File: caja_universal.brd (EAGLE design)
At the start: 136.8 x 101.5 mm, 45 parts, among them IC1 NE5534, IC2 AD620N, IC3 TL084P, IC4 TL084P, IC5 NE5534, IC6 TL072, J1 +12V-FUSE, J10 POT-OFFSET, J11 POT-GAIN, J12 I-PLACA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

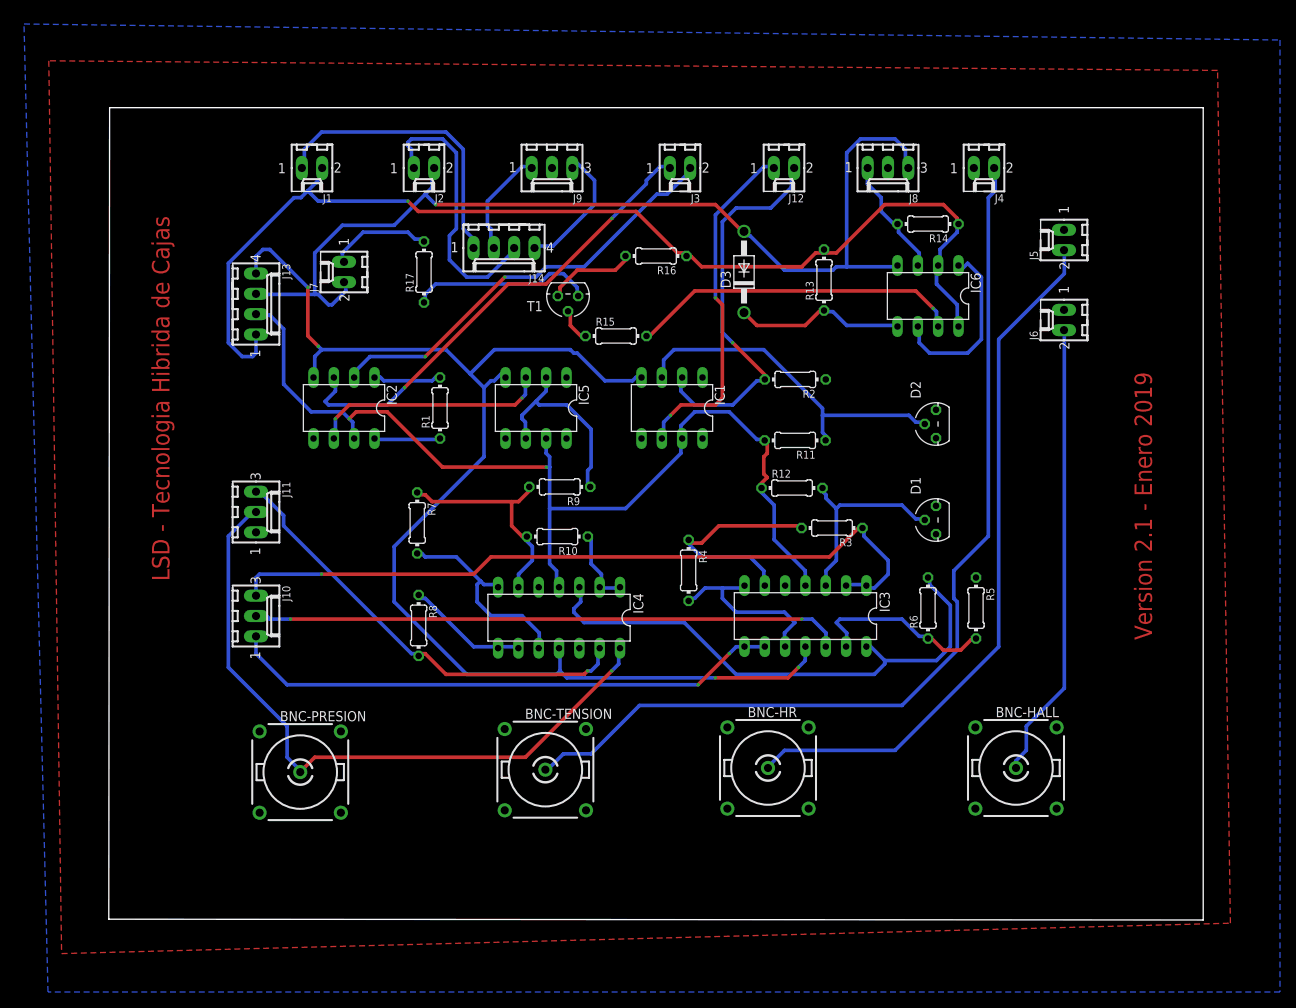
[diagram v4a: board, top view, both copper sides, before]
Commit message: Version para imprimir, routeada completa con tRestrict en zocalos y conectores
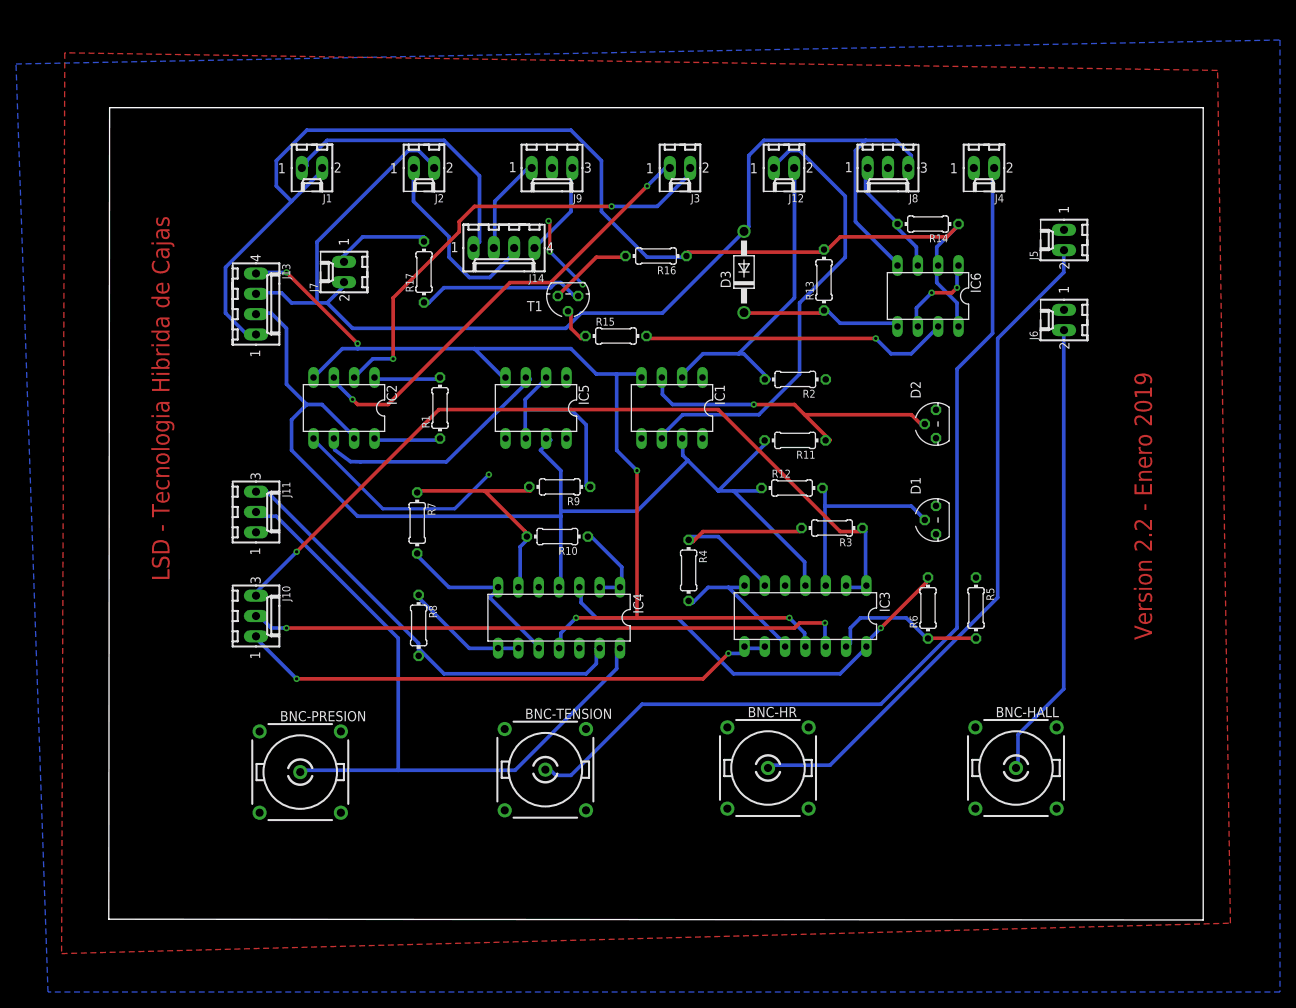
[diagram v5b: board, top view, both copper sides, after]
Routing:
- net 0V: track 0.00 -> 37.1 mm, vias 0 -> 4
- net V-: track 167.0 -> 133.9 mm, vias 4 -> 5
- net -12V: track 128.7 -> 151.7 mm, vias 1 -> 0
- net V+: track 128.4 -> 144.0 mm, vias 2 -> 0
- net N$11: track 68.9 -> 54.8 mm, vias 0 -> 1
- net +I: track 43.8 -> 57.7 mm, vias 2 -> 0
- net N$21: track 23.4 -> 11.3 mm, vias 0 -> 2
- net -12VFUSE: track 35.0 -> 24.1 mm
- net -I: track 49.4 -> 40.2 mm, vias 1 -> 0
- net +12V: track 139.3 -> 148.5 mm, vias 1 -> 0
- net 1.25V: track 94.3 -> 102.3 mm
- net -12VBAT: track 17.2 -> 11.9 mm
- net P-: track 53.7 -> 58.7 mm
- net N$8: track 23.0 -> 18.3 mm
- net HR: track 88.3 -> 84.5 mm
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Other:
- board text added: "Version 2.2 - Enero 2019"
- board text removed: "Version 2.1 - Enero 2019"

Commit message: Genero gerber files
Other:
- board size 136.8 x 101.5 mm -> 136 x 101 mm
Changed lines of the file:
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@@
 <setting verticaltext="up"/>
 </settings>
-<grid distance="6" unitdist="mil" unit="mil" style="lines" multiple="1" display="yes" altdistance="39.3700787" altunitdist="mil" altunit="mil"/>
+<grid distance="1" unitdist="mm" unit="mm" style="lines" multiple="1" display="yes" altdistance="39.3700787" altunitdist="mil" altunit="mil"/>
 <layers>
-<layer number="1" name="Top" color="4" fill="1" visible="yes" active="yes"/>
+<layer number="1" name="Top" color="4" fill="1" visible="no" active="yes"/>
 <layer number="16" name="Bottom" color="1" fill="1" visible="no" active="yes"/>
-<layer number="17" name="Pads" color="2" fill="1" visible="yes" active="yes"/>
-<layer number="18" name="Vias" color="2" fill="1" visible="yes" active="yes"/>
-<layer number="19" name="Unrouted" color="6" fill="1" visible="yes" active="yes"/>
-<layer number="20" name="Dimension" color="15" fill="1" visible="yes" active="yes"/>
-<layer number="21" name="tPlace" color="7" fill="1" visible="yes" active="yes"/>
-<layer number="22" name="bPlace" color="7" fill="1" visible="yes" active="yes"/>
-<layer number="23" name="tOrigins" color="15" fill="1" visible="yes" active="yes"/>
-<layer number="24" name="bOrigins" color="15" fill="1" visible="yes" active="yes"/>
+<layer number="17" name="Pads" color="2" fill="1" visible="no" active="yes"/>
+<layer number="18" name="Vias" color="2" fill="1" visible="no" active="yes"/>
+<layer number="19" name="Unrouted" color="6" fill="1" visible="no" active="yes"/>
+<layer number="20" name="Dimension" color="15" fill="1" visible="no" active="yes"/>
+<layer number="21" name="tPlace" color="7" fill="1" visible="no" active="yes"/>
+<layer number="22" name="bPlace" color="7" fill="1" visible="no" active="yes"/>
+<layer number="23" name="tOrigins" color="15" fill="1" visible="no" active="yes"/>
+<layer number="24" name="bOrigins" color="15" fill="1" visible="no" active="yes"/>
 <layer number="25" name="tNames" color="7" fill="1" visible="yes" active="yes"/>
-<layer number="26" name="bNames" color="7" fill="1" visible="yes" active="yes"/>
-<layer number="27" name="tValues" color="7" fill="1" visible="yes" active="yes"/>
-<layer number="28" name="bValues" color="7" fill="1" visible="yes" active="yes"/>
-<layer number="29" name="tStop" color="7" fill="3" visible="yes" active="yes"/>
-<layer number="30" name="bStop" color="7" fill="6" visible="yes" active="yes"/>
-<layer number="31" name="tCream" color="7" fill="4" visible="yes" active="yes"/>
-<layer number="32" name="bCream" color="7" fill="5" visible="yes" active="yes"/>
-<layer number="33" name="tFinish" color="6" fill="3" visible="yes" active="yes"/>
-<layer number="34" name="bFinish" color="6" fill="6" visible="yes" active="yes"/>
-<layer number="35" name="tGlue" color="7" fill="4" visible="yes" active="yes"/>
-<layer number="36" name="bGlue" color="7" fill="5" visible="yes" active="yes"/>
-<layer number="37" name="tTest" color="7" fill="1" visible="yes" active="yes"/>
-<layer number="38" name="bTest" color="7" fill="1" visible="yes" active="yes"/>
-<layer number="39" name="tKeepout" color="4" fill="11" visible="yes" active="yes"/>
-<layer number="40" name="bKeepout" color="1" fill="11" visible="yes" active="yes"/>
-<layer number="41" name="tRestrict" color="4" fill="10" visible="yes" active="yes"/>
-<layer number="42" name="bRestrict" color="1" fill="10" visible="yes" active="yes"/>
-<layer number="43" name="vRestrict" color="2" fill="10" visible="yes" active="yes"/>
-<layer number="44" name="Drills" color="7" fill="1" visible="yes" active="yes"/>
-<layer number="45" name="Holes" color="7" fill="1" visible="yes" active="yes"/>
-<layer number="46" name="Milling" color="3" fill="1" visible="yes" active="yes"/>
-<layer number="47" name="Measures" color="7" fill="1" visible="yes" active="yes"/>
-<layer number="48" name="Document" color="7" fill="1" visible="yes" active="yes"/>
-<layer number="49" name="Reference" color="7" fill="1" visible="yes" active="yes"/>
-<layer number="51" name="tDocu" color="7" fill="1" visible="yes" active="yes"/>
-<layer number="52" name="bDocu" color="7" fill="1" visible="yes" active="yes"/>
+<layer number="26" name="bNames" color="7" fill="1" visible="no" active="yes"/>
+<layer number="27" name="tValues" color="7" fill="1" visible="no" active="yes"/>
+<layer number="28" name="bValues" color="7" fill="1" visible="no" active="yes"/>
+<layer number="29" name="tStop" color="7" fill="3" visible="no" active="yes"/>
+<layer number="30" name="bStop" color="7" fill="6" visible="no" active="yes"/>
+<layer number="31" name="tCream" color="7" fill="4" visible="no" active="yes"/>
+<layer number="32" name="bCream" color="7" fill="5" visible="no" active="yes"/>
+<layer number="33" name="tFinish" color="6" fill="3" visible="no" active="yes"/>
+<layer number="34" name="bFinish" color="6" fill="6" visible="no" active="yes"/>
+<layer number="35" name="tGlue" color="7" fill="4" visible="no" active="yes"/>
+<layer number="36" name="bGlue" color="7" fill="5" visible="no" active="yes"/>
+<layer number="37" name="tTest" color="7" fill="1" visible="no" active="yes"/>
+<layer number="38" name="bTest" color="7" fill="1" visible="no" active="yes"/>
+<layer number="39" name="tKeepout" color="4" fill="11" visible="no" active="yes"/>
+<layer number="40" name="bKeepout" color="1" fill="11" visible="no" active="yes"/>
+<layer number="41" name="tRestrict" color="4" fill="10" visible="no" active="yes"/>
+<layer number="42" name="bRestrict" color="1" fill="10" visible="no" active="yes"/>
+<layer number="43" name="vRestrict" color="2" fill="10" visible="no" active="yes"/>
+<layer number="44" name="Drills" color="7" fill="1" visible="no" active="yes"/>
+<layer number="45" name="Holes" color="7" fill="1" visible="no" active="yes"/>
+<layer number="46" name="Milling" color="3" fill="1" visible="no" active="yes"/>
+<layer number="47" name="Measures" color="7" fill="1" visible="no" active="yes"/>
+<layer number="48" name="Document" color="7" fill="1" visible="no" active="yes"/>
+<layer number="49" name="Reference" color="7" fill="1" visible="no" active="yes"/>
+<layer number="51" name="tDocu" color="7" fill="1" visible="no" active="yes"/>
+<layer number="52" name="bDocu" color="7" fill="1" visible="no" active="yes"/>
 <layer number="90" name="Modules" color="5" fill="1" visible="no" active="no"/>
 <layer number="91" name="Nets" color="2" fill="1" visible="no" active="no"/>
@@
 <board>
 <plain>
-<wire x1="-18.4" y1="-12.9" x2="118.4" y2="-13" width="0" layer="20"/>
-<wire x1="118.4" y1="-13" x2="118.4" y2="88.54" width="0" layer="20"/>
-<wire x1="118.4" y1="88.54" x2="-18.3" y2="88.54" width="0" layer="20"/>
-<wire x1="-18.3" y1="88.54" x2="-18.4" y2="-12.9" width="0" layer="20"/>
-<text x="-13" y="75" size="2.1844" layer="1" font="vector" rot="R270">LSD - Tecnologia Hibrida de Cajas</text>
-<text x="112" y="22" size="2.1844" layer="1" font="vector" rot="R90">Version 2.2 - Enero 2019</text>
+<wire x1="-18" y1="-13" x2="118" y2="-13" width="0" layer="20"/>
+<wire x1="118" y1="-13" x2="118" y2="88" width="0" layer="20"/>
+<wire x1="118" y1="88" x2="-18" y2="88" width="0" layer="20"/>
+<wire x1="-18" y1="88" x2="-18" y2="-13" width="0" layer="20"/>
+<text x="-13" y="75" size="2.1844" layer="25" font="vector" rot="R270">LSD - Tecnologia Hibrida de Cajas</text>
+<text x="112" y="21" size="2.1844" layer="25" font="vector" rot="R90">Version 2.2 - Enero 2019</text>
 <polygon width="0.4064" layer="41">
 <vertex x="-3" y="69"/>
@@
 <vertex x="29" y="27"/>
 </polygon>
+<hole x="-14" y="-9" drill="0.6"/>
+<hole x="-14" y="84" drill="0.6"/>
+<hole x="114" y="84" drill="0.6"/>
+<hole x="114" y="-9" drill="0.6"/>
 </plain>
 <attributes>
@@
 <contactref element="BNC-HR" pad="5"/>
 <polygon width="0.4064" layer="1">
-<vertex x="-24.3" y="-17.2"/>
-<vertex x="121.8" y="-13.4"/>
-<vertex x="120.2" y="93.2"/>
-<vertex x="-23.9" y="95.4"/>
+<vertex x="-25" y="-18"/>
+<vertex x="123" y="-17"/>
+<vertex x="123" y="92"/>
+<vertex x="-25" y="92"/>
 </polygon>
 <contactref element="D1" pad="FB"/>
@@
 <contactref element="D2" pad="-"/>
 <polygon width="0.8128" layer="16">
-<vertex x="-30" y="94"/>
-<vertex x="128" y="97"/>
-<vertex x="128" y="-22"/>
-<vertex x="-26" y="-22"/>
+<vertex x="-24" y="91"/>
+<vertex x="122" y="91"/>
+<vertex x="122" y="-16"/>
+<vertex x="-24" y="-17"/>
 </polygon>
 <contactref element="IC4" pad="12"/>

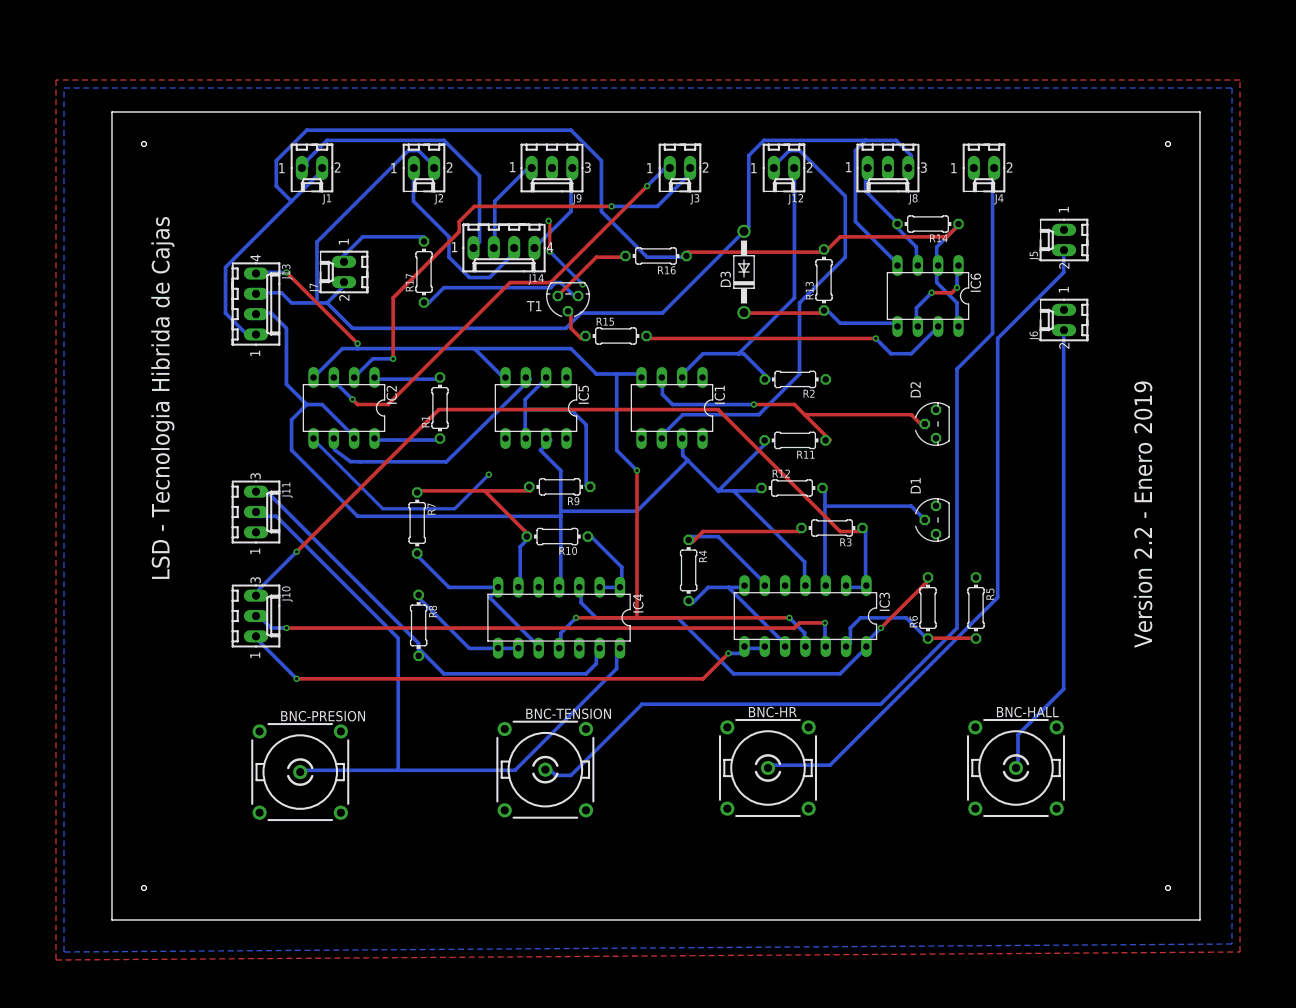
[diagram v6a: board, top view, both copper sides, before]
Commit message: Modifico para reducir tamaño debajo de 100x100 (precio impresion); genero gerbers nuevos: ENVIAR
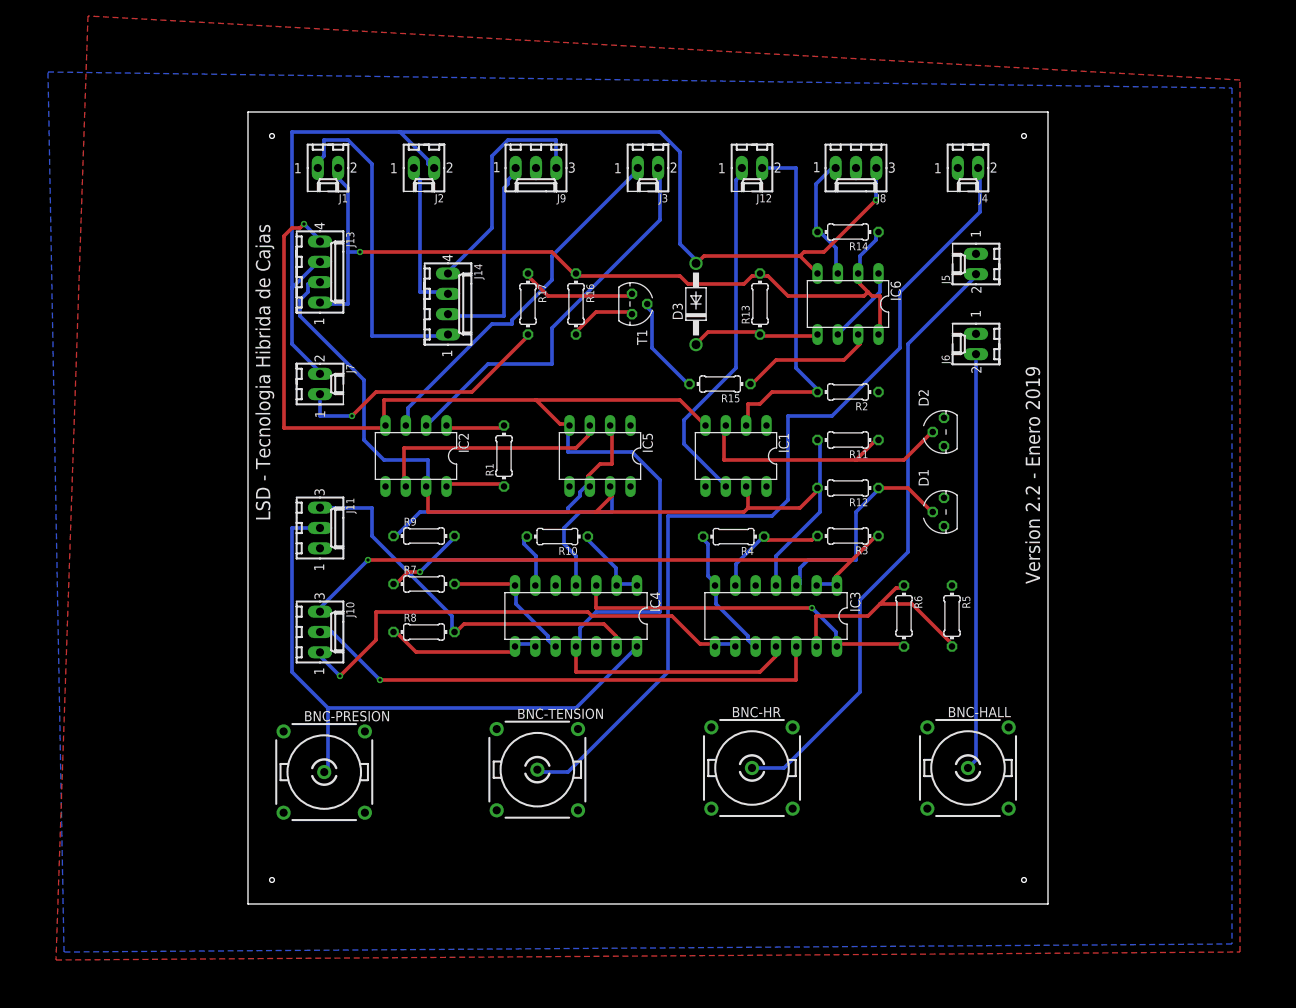
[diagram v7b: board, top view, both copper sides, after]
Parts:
- moved R9 18.0 mm to (21.0, 35.0), turned to 0 degrees
- moved J7 14.3 mm to (8.00, 54.0), turned to 270 degrees
- moved R15 14.3 mm to (58.0, 54.0)
- moved R17 13.6 mm to (34.0, 64.0), turned to 270 degrees
- moved R16 11.7 mm to (40.0, 64.0), turned to 270 degrees
- moved J5 11.4 mm to (90.0, 69.0)
- moved J6 11.4 mm to (90.0, 59.0)
- moved IC2 10.8 mm to (20.0, 45.0)
- moved IC6 10.0 mm to (74.0, 64.0)
- moved R14 10.0 mm to (74.0, 73.0)
- moved IC1 10.0 mm to (60.0, 45.0)
- moved IC5 10.0 mm to (43.0, 45.0)
- moved R1 10.0 mm to (31.0, 45.0)
- moved J14 9.90 mm to (24.0, 64.0), turned to 270 degrees
- moved J13 8.94 mm to (8.00, 68.0)
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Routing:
- net +12V: track 148.5 -> 106.1 mm, vias 0 -> 1
- net 0V: track 37.1 -> 0.00 mm, vias 4 -> 0
- net V-: track 133.9 -> 169.7 mm, vias 5 -> 1
- net N$24: track 38.9 -> 17.1 mm, vias 1 -> 0
- net 1.25V: track 102.3 -> 80.7 mm
- net CHECK-LED: track 12.4 -> 33.1 mm, vias 0 -> 1
- net -12VBAT: track 11.9 -> 29.3 mm
- net +12VBAT: track 12.5 -> 26.6 mm
- net N$6: track 27.7 -> 14.8 mm
- net N$13: track 25.2 -> 37.9 mm
- net +I: track 57.7 -> 45.1 mm
- net -12V: track 151.7 -> 140.7 mm, vias 0 -> 1
- net POUT: track 89.0 -> 78.2 mm
- net P+: track 56.2 -> 45.8 mm, vias 2 -> 0
- net N$11: track 54.8 -> 44.7 mm
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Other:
- board size 136 x 101 mm -> 100 x 99 mm
